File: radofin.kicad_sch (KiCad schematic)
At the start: 6 parts, among them J1 Conn_02x16_Counter_Clockwise, SW2 SW_DIP_x03, U1 27C128

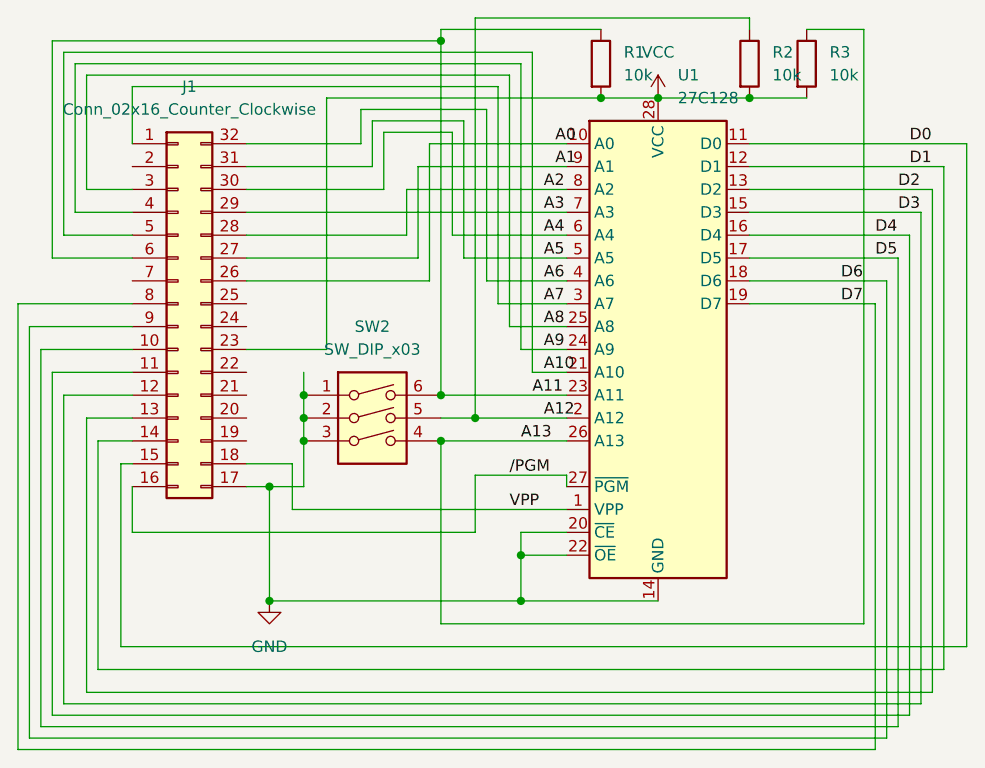
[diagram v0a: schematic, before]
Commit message: Rewiring after an optical review
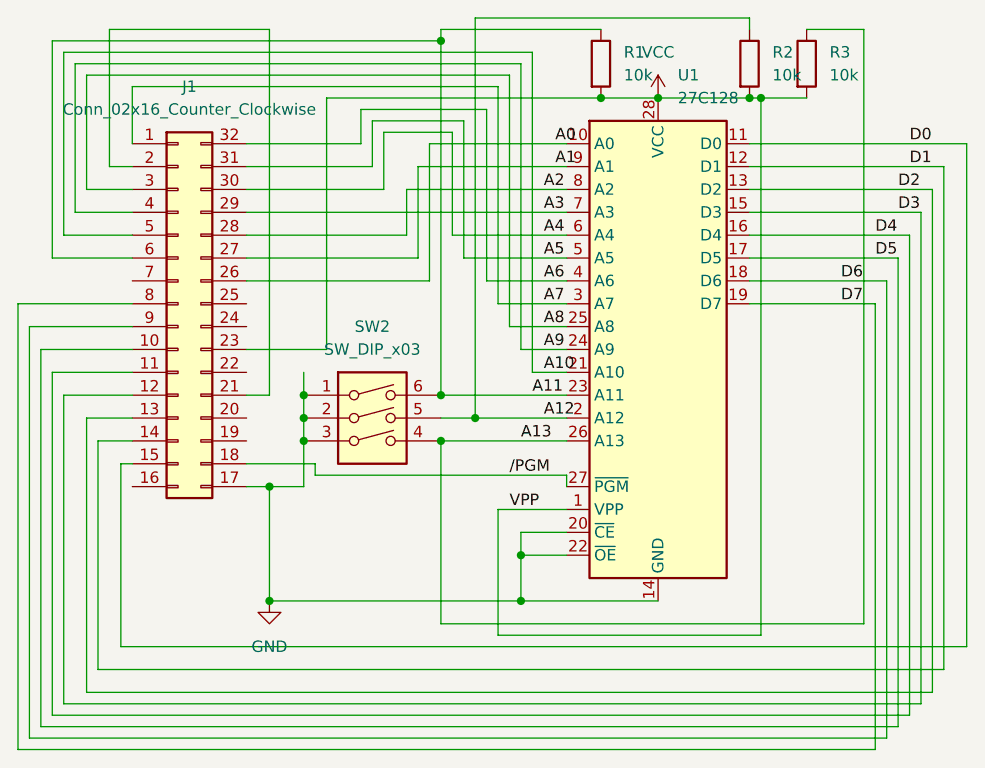
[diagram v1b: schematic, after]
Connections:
- net VCC: now also U1.1 (VPP)
- net /PGM: now also J1.18 (Pin_18); no longer J1.16 (Pin_16)
- net at J1.2 (Pin_2): now also J1.21 (Pin_21)
- removed net VPP: J1.18 (Pin_18), U1.1 (VPP)
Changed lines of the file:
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@@
   (junction (at 93.98 78.74) (diameter 0) (color 0 0 0 0)
   )
+  (junction (at 144.78 40.64) (diameter 0) (color 0 0 0 0)
+  )
   (junction (at 143.51 40.64) (diameter 0) (color 0 0 0 0)
   )
   (junction (at 118.11 96.52) (diameter 0) (color 0 0 0 0)
   )
-  (wire (pts (xy 87.63 81.28) (xy 92.71 81.28))
+  (wire (pts (xy 90.17 73.66) (xy 87.63 73.66))
     (stroke (width 0) (type default))
   )
@@
     (stroke (width 0) (type default))
   )
-  (wire (pts (xy 74.93 83.82) (xy 74.93 88.9))
-    (stroke (width 0) (type default))
-  )
   (wire (pts (xy 87.63 55.88) (xy 105.41 55.88))
     (stroke (width 0) (type default))
@@
     (stroke (width 0) (type default))
   )
+  (wire (pts (xy 72.39 33.02) (xy 90.17 33.02))
+    (stroke (width 0) (type default))
+  )
   (wire (pts (xy 111.76 58.42) (xy 111.76 43.18))
     (stroke (width 0) (type default))
@@
     (stroke (width 0) (type default))
   )
+  (wire (pts (xy 123.19 86.36) (xy 115.57 86.36))
+    (stroke (width 0) (type default))
+  )
   (wire (pts (xy 123.19 71.12) (xy 119.38 71.12))
     (stroke (width 0) (type default))
@@
     (stroke (width 0) (type default))
   )
-  (wire (pts (xy 143.51 40.64) (xy 149.86 40.64))
+  (wire (pts (xy 143.51 40.64) (xy 144.78 40.64))
     (stroke (width 0) (type default))
   )
@@
     (stroke (width 0) (type default))
   )
+  (wire (pts (xy 90.17 33.02) (xy 90.17 73.66))
+    (stroke (width 0) (type default))
+  )
   (wire (pts (xy 143.51 53.34) (xy 162.56 53.34))
     (stroke (width 0) (type default))
@@
     (stroke (width 0) (type default))
   )
-  (wire (pts (xy 113.03 88.9) (xy 113.03 82.55))
-    (stroke (width 0) (type default))
-  )
   (wire (pts (xy 118.11 91.44) (xy 123.19 91.44))
     (stroke (width 0) (type default))
@@
     (stroke (width 0) (type default))
   )
+  (wire (pts (xy 115.57 86.36) (xy 115.57 100.33))
+    (stroke (width 0) (type default))
+  )
   (wire (pts (xy 109.22 73.66) (xy 123.19 73.66))
     (stroke (width 0) (type default))
   )
-  (wire (pts (xy 92.71 86.36) (xy 123.19 86.36))
-    (stroke (width 0) (type default))
-  )
   (wire (pts (xy 87.63 53.34) (xy 123.19 53.34))
     (stroke (width 0) (type default))
@@
     (stroke (width 0) (type default))
   )
+  (wire (pts (xy 87.63 81.28) (xy 95.25 81.28))
+    (stroke (width 0) (type default))
+  )
   (wire (pts (xy 100.33 41.91) (xy 114.3 41.91))
     (stroke (width 0) (type default))
@@
     (stroke (width 0) (type default))
   )
+  (wire (pts (xy 115.57 100.33) (xy 144.78 100.33))
+    (stroke (width 0) (type default))
+  )
   (wire (pts (xy 123.19 58.42) (xy 111.76 58.42))
     (stroke (width 0) (type default))
@@
     (stroke (width 0) (type default))
   )
-  (wire (pts (xy 113.03 82.55) (xy 123.19 82.55))
+  (wire (pts (xy 95.25 82.55) (xy 123.19 82.55))
     (stroke (width 0) (type default))
   )
@@
     (stroke (width 0) (type default))
   )
+  (wire (pts (xy 144.78 40.64) (xy 149.86 40.64))
+    (stroke (width 0) (type default))
+  )
   (wire (pts (xy 165.1 104.14) (xy 71.12 104.14))
     (stroke (width 0) (type default))
@@
     (stroke (width 0) (type default))
   )
+  (wire (pts (xy 74.93 48.26) (xy 72.39 48.26))
+    (stroke (width 0) (type default))
+  )
   (wire (pts (xy 143.51 63.5) (xy 157.48 63.5))
     (stroke (width 0) (type default))
@@
     (stroke (width 0) (type default))
   )
-  (wire (pts (xy 74.93 88.9) (xy 113.03 88.9))
+  (wire (pts (xy 72.39 48.26) (xy 72.39 33.02))
     (stroke (width 0) (type default))
   )
@@
     (stroke (width 0) (type default))
   )
-  (wire (pts (xy 92.71 81.28) (xy 92.71 86.36))
-    (stroke (width 0) (type default))
-  )
+  (wire (pts (xy 144.78 40.64) (xy 144.78 100.33))
+    (stroke (width 0) (type default))
+  )
+  (wire (pts (xy 95.25 81.28) (xy 95.25 82.55))
+    (stroke (width 0) (type default))
+  )
